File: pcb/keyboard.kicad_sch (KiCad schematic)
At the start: 50 parts, among them J1 TRRS, SW11 1, SW12 2, SW13 3, SW14 4, SW15 5, SW16 6, SW17 7, SW18 8, SW19 9, SW21 11, SW22 12, SW23 13, SW24 14, SW25 15, SW26 16, SW27 17, SW28 18, SW29 19, SW31 21, SW32 22, SW33 23, SW34 24, SW35 25, SW36 26, SW37 27, SW38 28, SW39 29, SW41 31, SW42 32, SW43 33, SW45 35, SW46 36, SW47 37, SW48 38, SW49 39, U1 EliteC

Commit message: fix switch references
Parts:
- SW11: value 1 -> 11
- SW12: value 2 -> 12
- SW13: value 3 -> 13
- SW14: value 4 -> 14
- SW15: value 5 -> 15
- SW16: value 6 -> 16
- SW17: value 7 -> 17
- SW18: value 8 -> 18
- SW19: value 9 -> 19
- SW21: value 11 -> 21
- SW22: value 12 -> 22
- SW23: value 13 -> 23
- SW24: value 14 -> 24
- SW25: value 15 -> 25
- SW26: value 16 -> 26
- SW27: value 17 -> 27
- SW28: value 18 -> 28
- SW29: value 19 -> 29
- SW31: value 21 -> 31
- SW32: value 22 -> 32
- SW33: value 23 -> 33
- SW34: value 24 -> 34
- SW35: value 25 -> 35
- SW36: value 26 -> 36
- SW37: value 27 -> 37
- SW38: value 28 -> 38
- SW39: value 29 -> 39
- SW41: value 31 -> 41
- SW42: value 32 -> 42
- SW43: value 33 -> 43
- SW45: value 35 -> 45
- SW46: value 36 -> 46
- SW47: value 37 -> 47
- SW48: value 38 -> 48
- SW49: value 39 -> 49
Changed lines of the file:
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@@
       (effects (font (size 1.27 1.27)))
     )
-    (property "Value" "2" (at 128.27 46.355 0) (do_not_autoplace)
+    (property "Value" "12" (at 128.27 46.355 0) (do_not_autoplace)
       (effects (font (size 1.27 1.27)) hide)
     )
@@
       (effects (font (size 1.27 1.27)))
     )
-    (property "Value" "24" (at 163.83 81.915 0) (do_not_autoplace)
+    (property "Value" "34" (at 163.83 81.915 0) (do_not_autoplace)
       (effects (font (size 1.27 1.27)) hide)
     )
@@
       (effects (font (size 1.27 1.27)))
     )
-    (property "Value" "27" (at 217.17 81.915 0) (do_not_autoplace)
+    (property "Value" "37" (at 217.17 81.915 0) (do_not_autoplace)
       (effects (font (size 1.27 1.27)) hide)
     )
@@
       (effects (font (size 1.27 1.27)))
     )
-    (property "Value" "33" (at 146.05 99.695 0) (do_not_autoplace)
+    (property "Value" "43" (at 146.05 99.695 0) (do_not_autoplace)
       (effects (font (size 1.27 1.27)) hide)
     )
@@
       (effects (font (size 1.27 1.27)))
     )
-    (property "Value" "31" (at 110.49 99.695 0) (do_not_autoplace)
+    (property "Value" "41" (at 110.49 99.695 0) (do_not_autoplace)
       (effects (font (size 1.27 1.27)) hide)
     )
@@
       (effects (font (size 1.27 1.27)))
     )
-    (property "Value" "7" (at 217.17 46.355 0) (do_not_autoplace)
+    (property "Value" "17" (at 217.17 46.355 0) (do_not_autoplace)
       (effects (font (size 1.27 1.27)) hide)
     )
@@
       (effects (font (size 1.27 1.27)))
     )
-    (property "Value" "26" (at 199.39 81.915 0) (do_not_autoplace)
+    (property "Value" "36" (at 199.39 81.915 0) (do_not_autoplace)
       (effects (font (size 1.27 1.27)) hide)
     )
@@
       (effects (font (size 1.27 1.27)))
     )
-    (property "Value" "17" (at 217.17 64.135 0) (do_not_autoplace)
+    (property "Value" "27" (at 217.17 64.135 0) (do_not_autoplace)
       (effects (font (size 1.27 1.27)) hide)
     )
@@
       (effects (font (size 1.27 1.27)))
     )
-    (property "Value" "19" (at 252.73 64.135 0) (do_not_autoplace)
+    (property "Value" "29" (at 252.73 64.135 0) (do_not_autoplace)
       (effects (font (size 1.27 1.27)) hide)
     )
@@
       (effects (font (size 1.27 1.27)))
     )
-    (property "Value" "4" (at 163.83 46.355 0) (do_not_autoplace)
+    (property "Value" "14" (at 163.83 46.355 0) (do_not_autoplace)
       (effects (font (size 1.27 1.27)) hide)
     )
@@
       (effects (font (size 1.27 1.27)))
     )
-    (property "Value" "12" (at 128.27 64.135 0) (do_not_autoplace)
+    (property "Value" "22" (at 128.27 64.135 0) (do_not_autoplace)
       (effects (font (size 1.27 1.27)) hide)
     )
@@
       (effects (font (size 1.27 1.27)))
     )
-    (property "Value" "23" (at 146.05 81.915 0) (do_not_autoplace)
+    (property "Value" "33" (at 146.05 81.915 0) (do_not_autoplace)
       (effects (font (size 1.27 1.27)) hide)
     )
@@
       (effects (font (size 1.27 1.27)))
     )
-    (property "Value" "39" (at 252.73 99.695 0) (do_not_autoplace)
+    (property "Value" "49" (at 252.73 99.695 0) (do_not_autoplace)
       (effects (font (size 1.27 1.27)) hide)
     )
@@
       (effects (font (size 1.27 1.27)))
     )
-    (property "Value" "1" (at 110.49 46.355 0) (do_not_autoplace)
+    (property "Value" "11" (at 110.49 46.355 0) (do_not_autoplace)
       (effects (font (size 1.27 1.27)) hide)
     )
@@
       (effects (font (size 1.27 1.27)))
     )
-    (property "Value" "29" (at 252.73 81.915 0) (do_not_autoplace)
+    (property "Value" "39" (at 252.73 81.915 0) (do_not_autoplace)
       (effects (font (size 1.27 1.27)) hide)
     )
@@
       (effects (font (size 1.27 1.27)))
     )
-    (property "Value" "16" (at 199.39 64.135 0) (do_not_autoplace)
+    (property "Value" "26" (at 199.39 64.135 0) (do_not_autoplace)
       (effects (font (size 1.27 1.27)) hide)
     )
@@
       (effects (font (size 1.27 1.27)))
     )
-    (property "Value" "35" (at 181.61 99.695 0) (do_not_autoplace)
+    (property "Value" "45" (at 181.61 99.695 0) (do_not_autoplace)
       (effects (font (size 1.27 1.27)) hide)
     )
@@
       (effects (font (size 1.27 1.27)))
     )
-    (property "Value" "15" (at 181.61 64.135 0) (do_not_autoplace)
+    (property "Value" "25" (at 181.61 64.135 0) (do_not_autoplace)
       (effects (font (size 1.27 1.27)) hide)
     )
@@
       (effects (font (size 1.27 1.27)))
     )
-    (property "Value" "11" (at 110.49 64.135 0) (do_not_autoplace)
+    (property "Value" "21" (at 110.49 64.135 0) (do_not_autoplace)
       (effects (font (size 1.27 1.27)) hide)
     )
@@
       (effects (font (size 1.27 1.27)))
     )
-    (property "Value" "22" (at 128.27 81.915 0) (do_not_autoplace)
+    (property "Value" "32" (at 128.27 81.915 0) (do_not_autoplace)
       (effects (font (size 1.27 1.27)) hide)
     )
@@
       (effects (font (size 1.27 1.27)))
     )
-    (property "Value" "25" (at 181.61 81.915 0) (do_not_autoplace)
+    (property "Value" "35" (at 181.61 81.915 0) (do_not_autoplace)
       (effects (font (size 1.27 1.27)) hide)
     )
@@
       (effects (font (size 1.27 1.27)))
     )
-    (property "Value" "13" (at 146.05 64.135 0) (do_not_autoplace)
+    (property "Value" "23" (at 146.05 64.135 0) (do_not_autoplace)
       (effects (font (size 1.27 1.27)) hide)
     )
@@
       (effects (font (size 1.27 1.27)))
     )
-    (property "Value" "21" (at 110.49 81.915 0) (do_not_autoplace)
+    (property "Value" "31" (at 110.49 81.915 0) (do_not_autoplace)
       (effects (font (size 1.27 1.27)) hide)
     )
@@
       (effects (font (size 1.27 1.27)))
     )
-    (property "Value" "6" (at 199.39 46.355 0) (do_not_autoplace)
+    (property "Value" "16" (at 199.39 46.355 0) (do_not_autoplace)
       (effects (font (size 1.27 1.27)) hide)
     )
@@
       (effects (font (size 1.27 1.27)))
     )
-    (property "Value" "36" (at 199.39 99.695 0) (do_not_autoplace)
+    (property "Value" "46" (at 199.39 99.695 0) (do_not_autoplace)
       (effects (font (size 1.27 1.27)) hide)
     )
@@
       (effects (font (size 1.27 1.27)))
     )
-    (property "Value" "18" (at 234.95 64.135 0) (do_not_autoplace)
+    (property "Value" "28" (at 234.95 64.135 0) (do_not_autoplace)
       (effects (font (size 1.27 1.27)) hide)
     )
@@
       (effects (font (size 1.27 1.27)))
     )
-    (property "Value" "3" (at 146.05 46.355 0) (do_not_autoplace)
+    (property "Value" "13" (at 146.05 46.355 0) (do_not_autoplace)
       (effects (font (size 1.27 1.27)) hide)
     )
@@
       (effects (font (size 1.27 1.27)))
     )
-    (property "Value" "28" (at 234.95 81.915 0) (do_not_autoplace)
+    (property "Value" "38" (at 234.95 81.915 0) (do_not_autoplace)
       (effects (font (size 1.27 1.27)) hide)
     )
@@
       (effects (font (size 1.27 1.27)))
     )
-    (property "Value" "38" (at 234.95 99.695 0) (do_not_autoplace)
+    (property "Value" "48" (at 234.95 99.695 0) (do_not_autoplace)
       (effects (font (size 1.27 1.27)) hide)
     )
@@
       (effects (font (size 1.27 1.27)))
     )
-    (property "Value" "9" (at 252.73 46.355 0) (do_not_autoplace)
+    (property "Value" "19" (at 252.73 46.355 0) (do_not_autoplace)
       (effects (font (size 1.27 1.27)) hide)
     )
@@
       (effects (font (size 1.27 1.27)))
     )
-    (property "Value" "14" (at 163.83 64.135 0) (do_not_autoplace)
+    (property "Value" "24" (at 163.83 64.135 0) (do_not_autoplace)
       (effects (font (size 1.27 1.27)) hide)
     )
@@
       (effects (font (size 1.27 1.27)))
     )
-    (property "Value" "37" (at 217.17 99.695 0) (do_not_autoplace)
+    (property "Value" "47" (at 217.17 99.695 0) (do_not_autoplace)
       (effects (font (size 1.27 1.27)) hide)
     )
@@
       (effects (font (size 1.27 1.27)))
     )
-    (property "Value" "8" (at 234.95 46.355 0) (do_not_autoplace)
+    (property "Value" "18" (at 234.95 46.355 0) (do_not_autoplace)
       (effects (font (size 1.27 1.27)) hide)
     )
@@
       (effects (font (size 1.27 1.27)))
     )
-    (property "Value" "5" (at 181.61 46.355 0) (do_not_autoplace)
+    (property "Value" "15" (at 181.61 46.355 0) (do_not_autoplace)
       (effects (font (size 1.27 1.27)) hide)
     )
@@
       (effects (font (size 1.27 1.27)))
     )
-    (property "Value" "32" (at 128.27 99.695 0) (do_not_autoplace)
-      (effects (font (size 1.27 1.27)) hide)
-    )
+    (property "Value" "42" (at 128.27 99.695 0) (do_not_autoplace)
+      (effects (font (size 1.27 1.27)) hide)
+    )

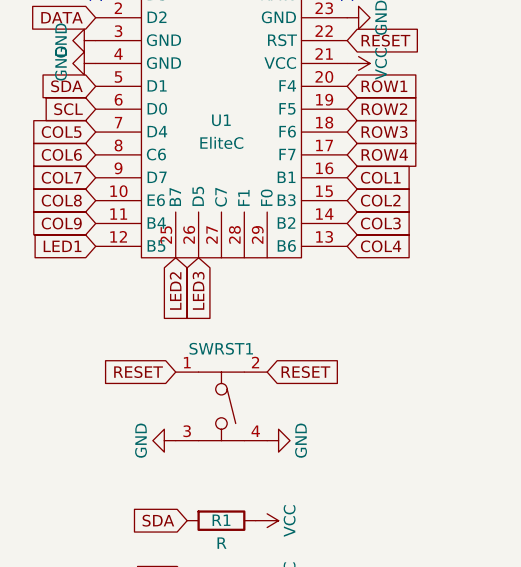
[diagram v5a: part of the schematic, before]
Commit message: add remaining bad traces
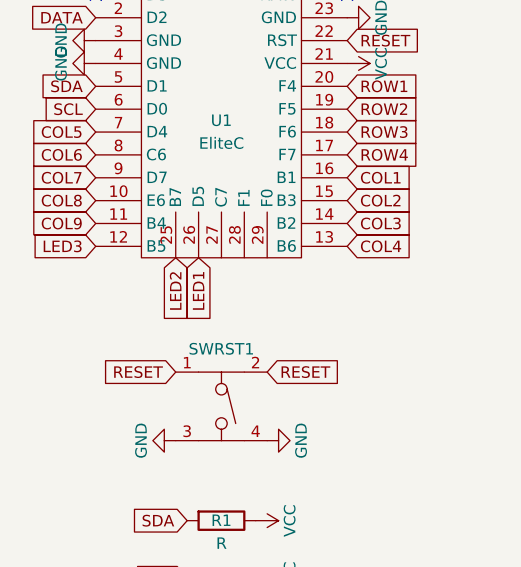
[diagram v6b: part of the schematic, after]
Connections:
- net LED1: now also U1.26 (D5); no longer U1.12 (B5)
- net LED3: now also U1.12 (B5); no longer U1.26 (D5)
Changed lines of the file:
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@@
-    )
-  )
-  (global_label "LED1" (shape input) (at 41.91 71.12 180) (fields_autoplaced)
-    (effects (font (size 1.27 1.27)) (justify right))
-    (property "Intersheetrefs" "${INTERSHEET_REFS}" (at 34.2682 71.12 0)
-      (effects (font (size 1.27 1.27)) (justify right) hide)
     )
   )
@@
     )
   )
+  (global_label "LED3" (shape input) (at 41.91 71.12 180) (fields_autoplaced)
+    (effects (font (size 1.27 1.27)) (justify right))
+    (property "Intersheetrefs" "${INTERSHEET_REFS}" (at 34.2682 71.12 0)
+      (effects (font (size 1.27 1.27)) (justify right) hide)
+    )
+  )
   (global_label "COL4" (shape input) (at 156.21 39.37 90) (fields_autoplaced)
     (effects (font (size 1.27 1.27)) (justify left))
@@
     )
   )
-  (global_label "LED3" (shape input) (at 53.34 72.39 270) (fields_autoplaced)
+  (global_label "LED1" (shape input) (at 53.34 72.39 270) (fields_autoplaced)
     (effects (font (size 1.27 1.27)) (justify right))
     (property "Intersheetrefs" "${INTERSHEET_REFS}" (at 53.34 80.0318 90)

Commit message: improve tracing around microcontroller
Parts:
- D1: renamed from LED1; value LED -> LED1
- D2: renamed from LED2; value LED -> LED2
- D3: renamed from LED3; value LED -> LED3
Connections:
- no-connect marks 2 -> 5
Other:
- moved on the sheet: U1

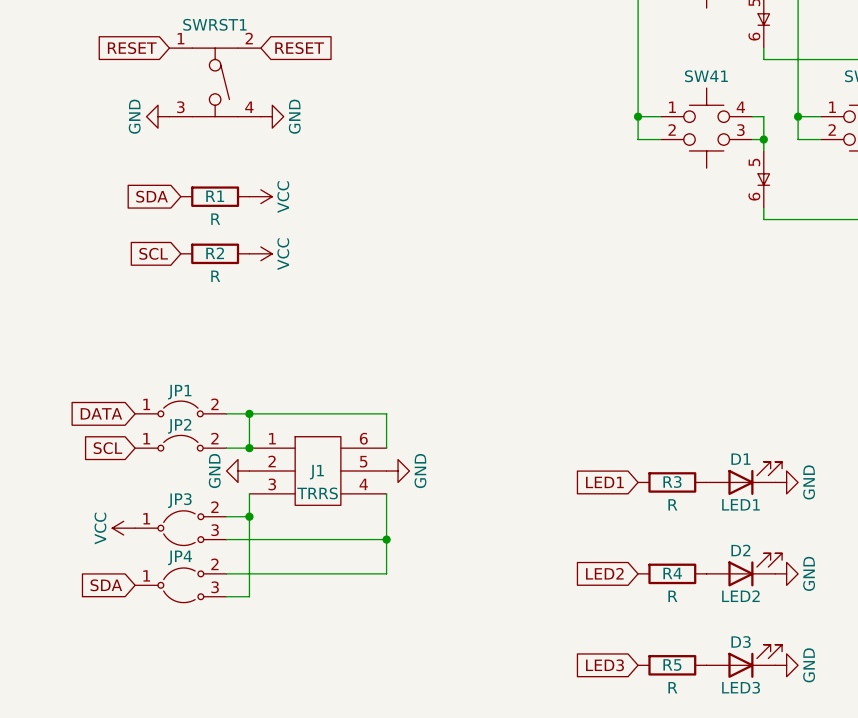
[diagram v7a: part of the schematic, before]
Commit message: fix silkscreen around microcontroller
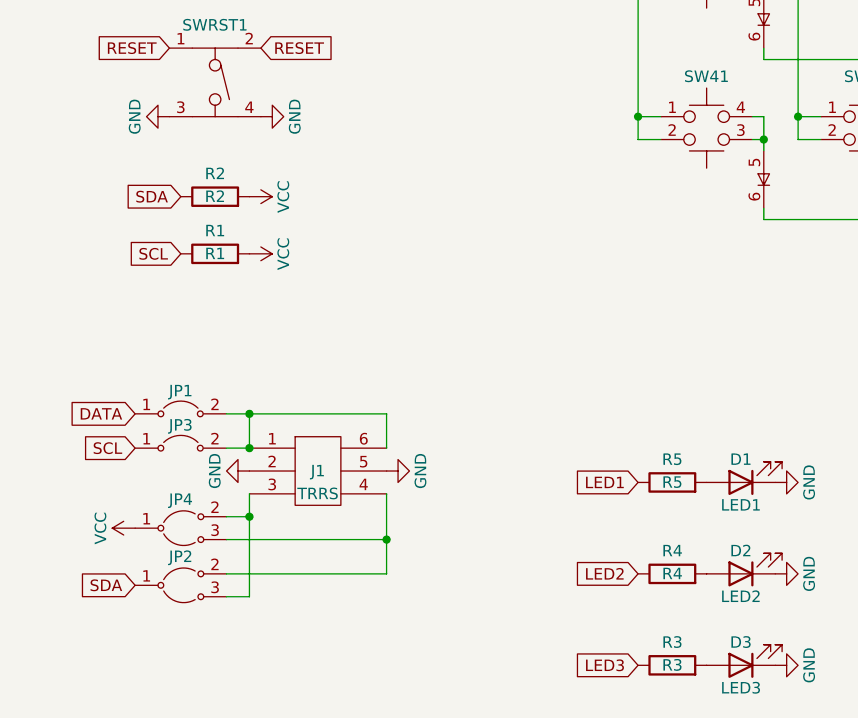
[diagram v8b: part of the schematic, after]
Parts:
- JP1: value Jumper -> J1
- JP2: renamed from JP4; value JumperSplit -> J2
- JP3: renamed from JP2; value Jumper -> J3
- JP4: renamed from JP3; value JumperSplit -> J4
- R1: value R -> R1
- R2: value R -> R2
- R3: value R -> R3
- R4: value R -> R4
- R5: value R -> R5
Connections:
- net LED1: now also R5.1; no longer R3.2
- net LED2: now also R4.1; no longer R4.2
- net LED3: now also R3.1; no longer R5.2
- net SCL: now also R1.1; no longer R2.2
- net SDA: now also R2.1; no longer R1.2
- net VCC: now also R1.2, R2.2; no longer R1.1, R2.1
- net at D2.2 (A): now also R4.2; no longer R4.1
- net at D3.2 (A): now also R3.2; no longer R5.1
- net at D1.2 (A): now also R5.2; no longer R3.1
